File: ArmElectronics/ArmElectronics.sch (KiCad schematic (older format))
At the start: 68 parts, among them J1 Raspberry_Pi_2_3, J2 Power In, Q1 BSS138, Q10 BSS138, Q11 BSS138, Q12 BSS138, Q13 BSS138, Q14 BSS138, Q15 BSS138, Q16 BSS138, Q17 BSS138, Q18 BSS138, Q2 BSS138, Q3 BSS138, Q4 BSS138, Q5 BSS138, Q6 BSS138, Q7 BSS138, Q8 BSS138, Q9 BSS138, U1 Teensy4.1, U10 PA-09, U2 Pololu_2857, U3 Pololu_2851, U4 BNO055_Adafruit_Breakout, U5 TB9051FTG, U6 TB9051FTG, U7 TB9051FTG, U8 PA-09, U9 PA-09

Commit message: Started footprints
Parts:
- removed Q10, Q11, Q12, Q13, Q14, Q15, Q16, Q17, Q18, Q2, Q3, Q4, Q5, Q6, Q7, Q8, Q9: BSS138, symbol Device:Q_NMOS_DGS
- added Q10, Q11, Q12, Q13, Q14, Q15, Q16, Q17, Q18, Q2, Q3, Q4, Q5, Q6, Q7, Q8, Q9: BSS138, Package_TO_SOT_SMD:SOT-23_Handsoldering, symbol Device:Q_NMOS_GSD
- Q1: footprint (none) -> Package_TO_SOT_SMD:SOT-23_Handsoldering; symbol Device:Q_NMOS_DGS -> Device:Q_NMOS_GSD
- R1, R10, R11, R12, R13, R14, R15, R16, R17, R18, R19, R2, R20, R21, R22, R23, R24, R25, R26, R27, R28, R29, R3, R30, R31, R32, R33, R34, R35, R36, R4, R5, R6, R7, R8, R9: footprint (none) -> Resistor_SMD:R_0603_1608Metric_Pad1.05x0.95mm_HandSolder
- R37: renamed from R?; footprint (none) -> Resistor_SMD:R_0603_1608Metric_Pad1.05x0.95mm_HandSolder
- gave numbers to parts that had none: 1

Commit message: Added 3 footprints
Added footprints for Pololu_2581, _2587, and TB9.
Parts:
- U2: footprint (none) -> ArmElectronics_Footprints:Pololu_2857
- U5, U6, U7: footprint (none) -> ArmElectronics_Footprints:TB9051FTG
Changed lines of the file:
@@
 EESchema Schematic File Version 4
+LIBS:ArmElectronics-cache
 EELAYER 30 0
 EELAYER END
@@
 F 0 "U5" H 12650 2115 50  0000 C CNN
 F 1 "TB9051FTG" H 12650 2024 50  0000 C CNN
-F 2 "" H 12600 2050 50  0001 C CNN
+F 2 "ArmElectronics_Footprints:TB9051FTG" H 12600 2050 50  0001 C CNN
 F 3 "" H 12600 2050 50  0001 C CNN
 	1    12550 1500
@@
 F 0 "U2" H 9300 2125 50  0000 C CNN
 F 1 "Pololu_2857" H 9300 2034 50  0000 C CNN
-F 2 "" H 9300 2050 50  0001 C CNN
+F 2 "ArmElectronics_Footprints:Pololu_2857" H 9300 2050 50  0001 C CNN
 F 3 "" H 9300 2050 50  0001 C CNN
 	1    9300 2050
@@
 F 0 "U6" H 12650 3765 50  0000 C CNN
 F 1 "TB9051FTG" H 12650 3674 50  0000 C CNN
-F 2 "" H 12600 3700 50  0001 C CNN
+F 2 "ArmElectronics_Footprints:TB9051FTG" H 12600 3700 50  0001 C CNN
 F 3 "" H 12600 3700 50  0001 C CNN
 	1    12550 3150
@@
 F 0 "U7" H 12650 5365 50  0000 C CNN
 F 1 "TB9051FTG" H 12650 5274 50  0000 C CNN
-F 2 "" H 12600 5300 50  0001 C CNN
+F 2 "ArmElectronics_Footprints:TB9051FTG" H 12600 5300 50  0001 C CNN
 F 3 "" H 12600 5300 50  0001 C CNN
 	1    12550 4750

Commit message: changed power architecture, moved bno to connector, associated footprints
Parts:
- removed U4: BNO055_Adafruit_Breakout, symbol ArmElectronics_Library:BNO055_Adafruit_Breakout
- added J4: Batt In, Connector_AMASS:AMASS_XT60-F_1x02_P7.20mm_Vertical, symbol Connector_Generic:Conn_01x02
- added J5: Batt Out, Connector_AMASS:AMASS_XT60-F_1x02_P7.20mm_Vertical, symbol Connector_Generic:Conn_01x02
- added J6: BNO055 QWIIC Conn, Connector_JST:JST_SH_SM04B-SRSS-TB_1x04-1MP_P1.00mm_Horizontal, symbol Connector_Generic:Conn_01x04
- J1: footprint (none) -> Connector_IDC:IDC-Header_2x20_P2.54mm_Vertical
- J2: value Power In -> 12V In; footprint (none) -> Connector_AMASS:AMASS_XT60-F_1x02_P7.20mm_Vertical
- J3: footprint (none) -> Connector_USB:USB_A_Molex_67643_Horizontal
- U1: footprint (none) -> ArmElectronics_Footprints:Teensy4.1
- U10, U8, U9: footprint (none) -> Connector_Molex:Molex_Mini-Fit_Jr_5566-06A_2x03_P4.20mm_Vertical
- U3: footprint (none) -> ArmElectronics_Footprints:Pololu_2851
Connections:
- net labels added: +BATT
- net labels removed: BNO055_RST
- wire segments 285 -> 288
- no-connect marks 23 -> 18
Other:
- moved on the sheet: J3, R37, U2, U3

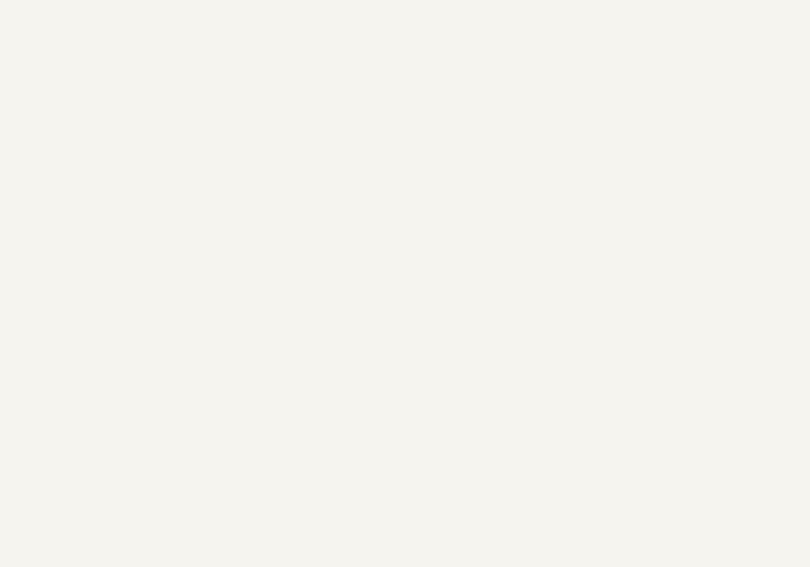
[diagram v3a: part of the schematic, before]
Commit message: added M3 mounting holes
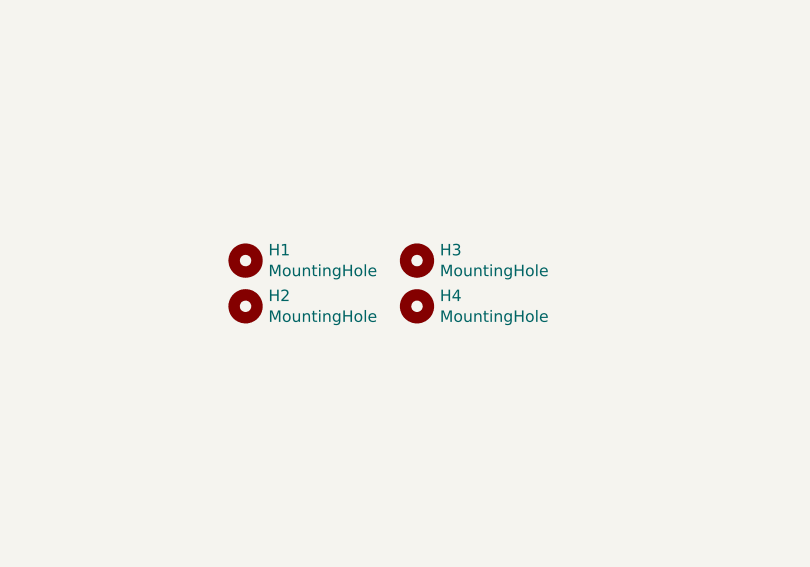
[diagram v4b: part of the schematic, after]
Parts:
- added H1, H2, H3, H4: MountingHole, MountingHole:MountingHole_3.2mm_M3, symbol Mechanical:MountingHole
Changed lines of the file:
@@
 Wire Wire Line
 	8900 7650 9450 7650
+$Comp
+L Mechanical:MountingHole H1
+U 1 1 5FD0D6DB
+P 2050 5900
+F 0 "H1" H 2150 5946 50  0000 L CNN
+F 1 "MountingHole" H 2150 5855 50  0000 L CNN
+F 2 "MountingHole:MountingHole_3.2mm_M3" H 2050 5900 50  0001 C CNN
+F 3 "~" H 2050 5900 50  0001 C CNN
+	1    2050 5900
+	1    0    0    -1
+$EndComp
+$Comp
+L Mechanical:MountingHole H2
+U 1 1 5FD0EC87
+P 2050 6100
+F 0 "H2" H 2150 6146 50  0000 L CNN
+F 1 "MountingHole" H 2150 6055 50  0000 L CNN
+F 2 "MountingHole:MountingHole_3.2mm_M3" H 2050 6100 50  0001 C CNN
+F 3 "~" H 2050 6100 50  0001 C CNN
+	1    2050 6100
+	1    0    0    -1
+$EndComp
+$Comp
+L Mechanical:MountingHole H3
+U 1 1 5FD0EE85
+P 2800 5900
+F 0 "H3" H 2900 5946 50  0000 L CNN
+F 1 "MountingHole" H 2900 5855 50  0000 L CNN
+F 2 "MountingHole:MountingHole_3.2mm_M3" H 2800 5900 50  0001 C CNN
+F 3 "~" H 2800 5900 50  0001 C CNN
+	1    2800 5900
+	1    0    0    -1
+$EndComp
+$Comp
+L Mechanical:MountingHole H4
+U 1 1 5FD0F27C
+P 2800 6100
+F 0 "H4" H 2900 6146 50  0000 L CNN
+F 1 "MountingHole" H 2900 6055 50  0000 L CNN
+F 2 "MountingHole:MountingHole_3.2mm_M3" H 2800 6100 50  0001 C CNN
+F 3 "~" H 2800 6100 50  0001 C CNN
+	1    2800 6100
+	1    0    0    -1
+$EndComp
 $EndSCHEMATC

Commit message: added part nums
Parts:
- J1: Additional Digikey Part Nums (none) -> 1528-2235-ND; Digikey Part Num (none) -> S9175-ND
- J2, J4, J5: Digikey Part Num (none) -> not on Digikey
- J3: Digikey Part Num (none) -> WM14667-ND
- J6: Digikey Part Num (none) -> 1528-4646-ND
- Q1, Q10, Q11, Q12, Q13, Q14, Q15, Q16, Q17, Q18, Q2, Q3, Q4, Q5, Q6, Q7, Q8, Q9: Digikey Part Num (none) -> BSS138CT-ND
- R1, R10, R11, R12, R13, R14, R15, R16, R17, R18, R19, R2, R20, R21, R22, R23, R24, R25, R26, R27, R28, R29, R3, R30, R31, R32, R33, R34, R35, R36, R4, R5, R6, R7, R8, R9: Digikey Part Num (none) -> P10KGCT-ND
- R37: Digikey Part Num (none) -> P200GCT-ND
- U1: Digikey Part Num (none) -> 1568-DEV-16996-ND
- U10, U8, U9: Digikey Part Num (none) -> WM3802-ND
- U2: Digikey Part Num (none) -> 2183-2857-ND
- U3: Digikey Part Num (none) -> 2183-2851-ND
- U5, U6, U7: Digikey Part Num (none) -> 2183-2997-ND

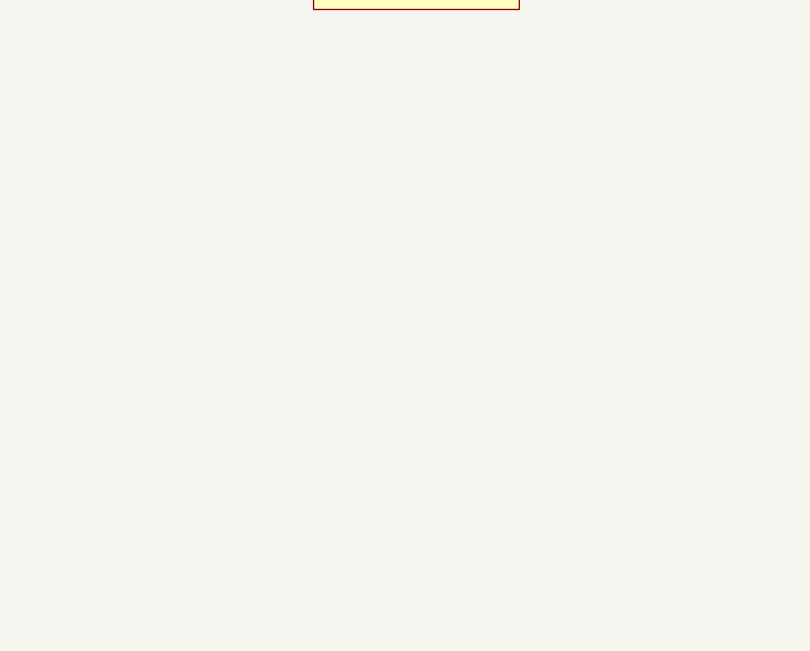
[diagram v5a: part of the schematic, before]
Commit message: Added some 3D models I found, started stepper driver
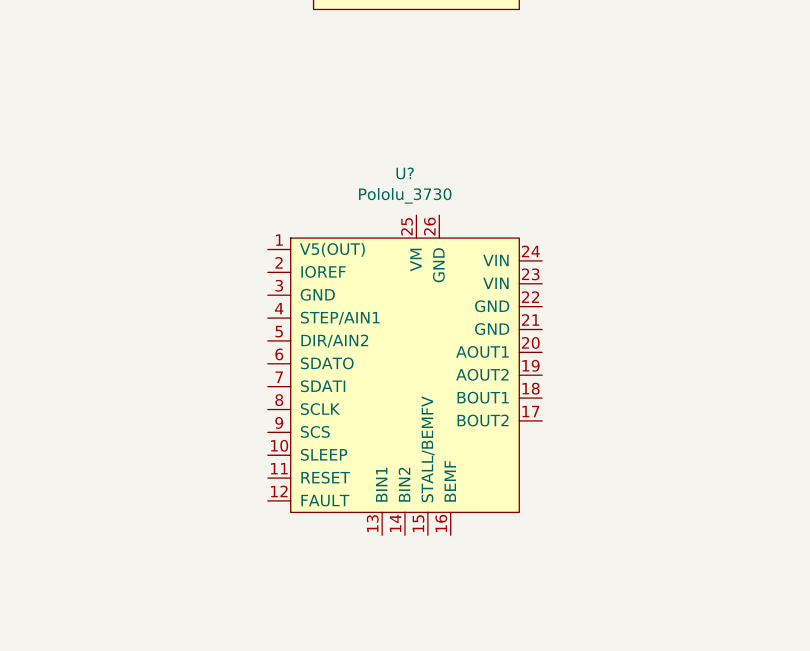
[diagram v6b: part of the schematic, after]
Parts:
- added U?: Pololu_3730, symbol ArmElectronics_Library:Pololu_3730
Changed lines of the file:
@@
+	1    0    0    -1
+$EndComp
+$Comp
+L ArmElectronics_Library:Pololu_3730 U?
+U 1 1 5FD37DEB
+P 12200 7050
+F 0 "U?" H 12600 7981 50  0000 C CNN
+F 1 "Pololu_3730" H 12600 7890 50  0000 C CNN
+F 2 "" H 12600 6200 50  0001 C CNN
+F 3 "" H 12600 6200 50  0001 C CNN
+	1    12200 7050
 	1    0    0    -1
 $EndComp

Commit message: I think the schematic is done?
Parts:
- added J7, J8: Conn_01x14, Connector_PinSocket_2.54mm:PinSocket_1x14_P2.54mm_Vertical, symbol Connector_Generic:Conn_01x14
- added J9: 1792245, Imported_Libraries:PHOENIX_1792245, symbol 1792245:1792245
- U4: renamed from U?; footprint (none) -> ArmElectronics_Footprints:Pololu_3730; Digikey Part Num (none) -> 2183-3730-ND
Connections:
- net +3V3: now also U4.10 (SLEEP), U4.2 (IOREF), J7.1 (Pin_1), J8.1 (Pin_1)
- net +5V: now also U1.30 (Vin)
- net +BATT: now also U4.23 (VIN), U4.24 (VIN)
- net GND: now also U1.1 (GND), U1.16 (GND), U1.29 (GND), U4.21 (GND), U4.22 (GND), U4.3 (GND), J7.2 (Pin_2), J8.2 (Pin_2)
- net M2_DIAG_3v: now also U1.25 (P21); no longer U1.11 (P9)
- net M2_HALL1_3v: now also U1.24 (P20); no longer U1.12 (P10)
- net M2_HALL2_3v: now also U1.23 (P19); no longer U1.13 (P11)
- net M2_PWM1_3v: now also U1.27 (P23); no longer U1.9 (P7)
- net M2_PWM2_3v: now also U1.26 (P22); no longer U1.10 (P8)
- net M3_DIAG_3v: now also U1.37 (P30); no longer U1.33 (P26)
- net M3_HALL1_3v: now also U1.38 (P31); no longer U1.34 (P27)
- net M3_HALL2_3v: now also U1.39 (P32); no longer U1.35 (P28)
- net M3_PWM1_3v: now also U1.35 (P28); no longer U1.31 (P24)
- net M3_PWM2_3v: now also U1.36 (P29); no longer U1.32 (P25)
- net RPi_SCL: now also J7.3 (Pin_3)
- net RPi_SDA: now also J7.4 (Pin_4)
- net RPi_GPI022: now reaches J1.15 (GPIO22)
- net RPi_GPI022: now also J7.11 (Pin_11)
- net RPi_GPIO23: now reaches J1.16 (GPIO23)
- net RPi_GPIO23: now also J7.12 (Pin_12)
- net RPi_GPIO24: now reaches J1.18 (GPIO24)
- net RPi_GPIO24: now also J7.13 (Pin_13)
- net RPi_MOSI0: now reaches J1.19 (MOSI0/GPIO10)
- net RPi_MOSI0: now also J7.6 (Pin_6)
- net RPi_MISO0: now reaches J1.21 (MISO0/GPIO9)
- net RPi_MISO0: now also J7.7 (Pin_7)
- net RPi_GPIO25: now reaches J1.22 (GPIO25)
- net RPi_GPIO25: now also J7.14 (Pin_14)
- net RPi_SCLK0: now reaches J1.23 (SCLK0/GPIO11)
- net RPi_SCLK0: now also J7.5 (Pin_5)
- net RPi_CS0: now reaches J1.24 (~CE0~/GPIO8)
- net RPi_CS0: now also J7.8 (Pin_8)
- net RPi_GPIO12: now reaches J1.32 (PWM0/GPIO12)
- net RPi_GPIO12: now also J7.9 (Pin_9)
- net RPi_GPIO13: now reaches J1.33 (PWM1/GPIO13)
- net RPi_GPIO13: now also J7.10 (Pin_10)
- net Teensy_MISO0: now reaches U1.14 (P12)
- net Teensy_MISO0: now also U4.6 (SDATO)
- net Teensy_SCK0: now reaches U1.17 (P13)
- net Teensy_SCK0: now also U4.8 (SCLK)
- net Stepper_BEMF: now reaches U1.21 (P17)
- net Stepper_BEMF: now also U4.16 (BEMF)
- net Stepper_Stall: now reaches U1.22 (P18)
- net Stepper_Stall: now also U4.15 (STALL/BEMFV)
- net Teensy_GPIO33: now reaches U1.40 (P33)
- net Teensy_GPIO33: now also J8.11 (Pin_11)
- net Teensy_GPIO34: now reaches U1.41 (P34)
- net Teensy_GPIO34: now also J8.12 (Pin_12)
- net Teensy_GPIO35: now reaches U1.42 (P35)
- net Teensy_GPIO35: now also J8.13 (Pin_13)
- net Teensy_GPIO36: now reaches U1.43 (P36)
- net Teensy_GPIO36: now also J8.9 (Pin_9)
- net Teensy_GPIO37: now reaches U1.44 (P37)
- net Teensy_GPIO37: now also J8.10 (Pin_10)
- net Teensy_CS1: now reaches U1.45 (P38)
- net Teensy_CS1: now also J8.8 (Pin_8)
- net Teensy_MISO1: now reaches U1.46 (P39)
- net Teensy_MISO1: now also J8.7 (Pin_7)
- net Teensy_GPIO40: now reaches U1.47 (P40)
- net Teensy_GPIO40: now also J8.14 (Pin_14)
- net Stepper_Fault: now reaches U4.12 (FAULT)
- net Stepper_Fault: now also U1.11 (P9)
- net at U4.17 (BOUT2): now also J9.4
- net at U4.18 (BOUT1): now also J9.3
- net at U4.19 (AOUT2): now also J9.2
- net at U4.20 (AOUT1): now also J9.1
- net Stepper_Step: now reaches U4.4 (STEP/AIN1)
- net Stepper_Step: now also U1.9 (P7)
- net Stepper_Dir: now reaches U4.5 (DIR/AIN2)
- net Stepper_Dir: now also U1.10 (P8)
- net Teensy_MOSI0: now reaches U4.7 (SDATI)
- net Teensy_MOSI0: now also U1.13 (P11)
- net Teensy_CS0: now reaches U4.9 (SCS)
- net Teensy_CS0: now also U1.12 (P10)
- new net Teensy_MOSI1: J8.6 (Pin_6), U1.33 (P26)
- new net Teensy_SCK1: J8.5 (Pin_5), U1.34 (P27)
- new net Teensy_SCL2: J8.3 (Pin_3), U1.31 (P24)
- new net Teensy_SDA2: J8.4 (Pin_4), U1.32 (P25)
- no-connect marks 18 -> 22

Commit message: Added additional part num
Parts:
- J6: Additional Digikey Part Nums (none) -> 455-1804-1-ND
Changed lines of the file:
@@
 F 3 "~" H 9650 7450 50  0001 C CNN
 F 4 "1528-4646-ND" H 9650 7450 50  0001 C CNN "Digikey Part Num"
+F 5 "455-1804-1-ND" H 9650 7450 50  0001 C CNN "Additional Digikey Part Nums"
 	1    9650 7450
 	1    0    0    -1
